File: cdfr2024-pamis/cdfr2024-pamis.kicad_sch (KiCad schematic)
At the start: 24 parts, among them J1 Connecteur batterie, J14 Conn_ST_STDC14, J4 Connecteur Programmation, J5 Connecteur Débug, J5 Connecteur ToF, J6 Moteur Droit, J7 Moteur Gauche, U1 LM317_SOT-223, U1 STM32F401RCTx, U4 Driver Moteur Droit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

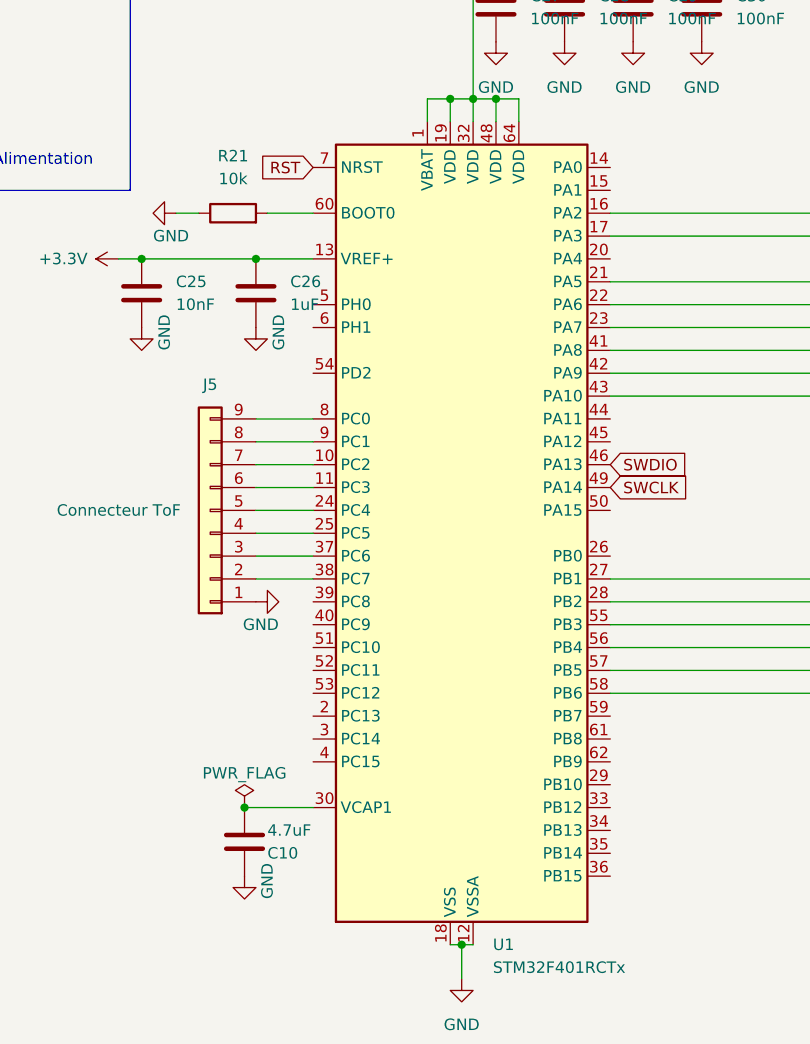
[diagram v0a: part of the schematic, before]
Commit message: - supression des messages d'erreur dans le schema - Suppression es message d'erreur sur PCB - modification des regles - modification du contour
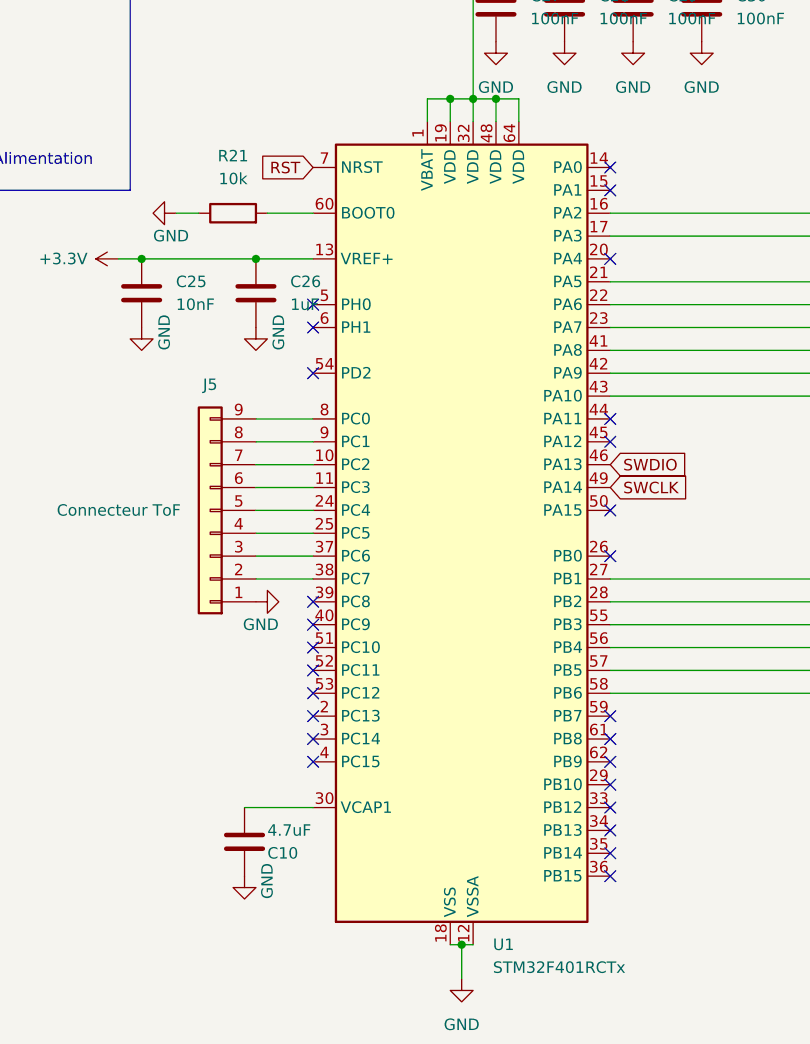
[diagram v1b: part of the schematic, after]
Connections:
- no-connect marks 4 -> 30
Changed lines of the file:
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@@
   (junction (at 146.05 46.99) (diameter 0) (color 0 0 0 0)
   )
-  (junction (at 123.19 125.73) (diameter 0) (color 0 0 0 0)
-  )
   (junction (at 60.96 48.26) (diameter 0) (color 0 0 0 0)
   )
@@
   (junction (at 34.29 25.4) (diameter 0) (color 0 0 0 0)
   )
+  (no_connect (at 163.83 118.11))
+  (no_connect (at 163.83 54.61))
+  (no_connect (at 163.83 115.57))
+  (no_connect (at 130.81 69.85))
   (no_connect (at 55.88 105.41))
+  (no_connect (at 130.81 105.41))
+  (no_connect (at 130.81 113.03))
+  (no_connect (at 163.83 97.79))
+  (no_connect (at 130.81 107.95))
+  (no_connect (at 163.83 82.55))
+  (no_connect (at 130.81 77.47))
+  (no_connect (at 130.81 118.11))
   (no_connect (at 71.12 92.71))
+  (no_connect (at 163.83 120.65))
+  (no_connect (at 163.83 57.15))
+  (no_connect (at 163.83 128.27))
+  (no_connect (at 163.83 85.09))
+  (no_connect (at 163.83 123.19))
+  (no_connect (at 163.83 64.77))
   (no_connect (at 71.12 87.63))
+  (no_connect (at 163.83 133.35))
+  (no_connect (at 163.83 125.73))
+  (no_connect (at 163.83 130.81))
+  (no_connect (at 163.83 92.71))
+  (no_connect (at 130.81 120.65))
+  (no_connect (at 130.81 102.87))
+  (no_connect (at 130.81 115.57))
   (no_connect (at 71.12 85.09))
+  (no_connect (at 130.81 110.49))
+  (no_connect (at 130.81 72.39))
   (wire (pts (xy 158.75 33.02) (xy 166.37 33.02))
     (stroke (width 0) (type default))
@@
         (path "/f2d064ab-e07d-4c4a-a207-b6758ac96116"
           (reference "#PWR010") (unit 1)
-        )
-      )
-    )
-  )
-  (symbol (lib_id "power:PWR_FLAG") (at 123.19 125.73 0) (unit 1)
-    (in_bom yes) (on_board yes) (dnp no)
-    (property "Reference" "#FLG0102" (at 123.19 123.825 0)
-      (effects (font (size 1.27 1.27)) hide)
-    )
-    (property "Value" "PWR_FLAG" (at 123.19 121.92 0)
-      (effects (font (size 1.27 1.27)))
-    )
-    (property "Footprint" "" (at 123.19 125.73 0)
-      (effects (font (size 1.27 1.27)) hide)
-    )
-    (property "Datasheet" "~" (at 123.19 125.73 0)
-      (effects (font (size 1.27 1.27)) hide)
-    )
-    (pin "1")
-    (instances
-      (project "Asservissement_CDFR_2023"
-        (path "/aba37299-4f54-471d-ab35-d760532fd54c"
-          (reference "#FLG0102") (unit 1)
-        )
-      )
-      (project "cdfr24_asservissement"
-        (path "/c6b82269-16f5-49e6-8b51-4d12a40a3077"
-          (reference "#FLG04") (unit 1)
-        )
-      )
-      (project "cdfr2024-pamis"
-        (path "/f2d064ab-e07d-4c4a-a207-b6758ac96116"
-          (reference "#FLG03") (unit 1)
         )
       )
@@
       (effects (font (size 1.27 1.27)) (justify bottom) hide)
     )
+    (pin "1")
+    (pin "10")
+    (pin "11")
+    (pin "12")
+    (pin "13")
+    (pin "14")
+    (pin "15")
+    (pin "16")
+    (pin "2")
     (pin "3")
-    (pin "15")
+    (pin "4")
+    (pin "5")
+    (pin "6")
     (pin "7")
-    (pin "12")
-    (pin "5")
-    (pin "1")
-    (pin "14")
-    (pin "11")
-    (pin "13")
-    (pin "16")
-    (pin "4")
     (pin "8")
-    (pin "2")
-    (pin "10")
-    (pin "6")
     (pin "9")
     (instances
@@
       (effects (font (size 1.27 1.27)) hide)
     )
-    (pin "2")
+    (pin "1")
+    (pin "2")
+    (pin "3")
     (pin "4")
-    (pin "3")
-    (pin "1")
     (instances
       (project "cdfr2024-pamis"
@@
       (effects (font (size 1.27 1.27)) hide)
     )
+    (pin "1")
+    (pin "10")
+    (pin "11")
+    (pin "12")
+    (pin "13")
+    (pin "14")
+    (pin "15")
+    (pin "16")
+    (pin "17")
+    (pin "18")
+    (pin "19")
+    (pin "2")
+    (pin "20")
+    (pin "21")
     (pin "22")
-    (pin "18")
+    (pin "23")
+    (pin "24")
+    (pin "25")
+    (pin "26")
     (pin "27")
+    (pin "28")
+    (pin "29")
+    (pin "3")
+    (pin "30")
+    (pin "31")
+    (pin "32")
+    (pin "33")
+    (pin "34")
     (pin "35")
     (pin "36")
-    (pin "3")
-    (pin "58")
-    (pin "10")
-    (pin "21")
+    (pin "37")
+    (pin "38")
+    (pin "39")
+    (pin "4")
+    (pin "40")
+    (pin "41")
+    (pin "42")
     (pin "43")
-    (pin "42")
-    (pin "6")
-    (pin "12")
-    (pin "62")
+    (pin "44")
+    (pin "45")
+    (pin "46")
+    (pin "47")
+    (pin "48")
     (pin "49")
-    (pin "54")
-    (pin "57")
-    (pin "61")
-    (pin "20")
-    (pin "16")
-    (pin "28")
-    (pin "30")
-    (pin "25")
-    (pin "4")
-    (pin "37")
-    (pin "39")
-    (pin "40")
-    (pin "48")
-    (pin "29")
-    (pin "14")
-    (pin "15")
-    (pin "31")
-    (pin "47")
+    (pin "5")
     (pin "50")
     (pin "51")
-    (pin "26")
-    (pin "33")
-    (pin "24")
     (pin "52")
-    (pin "46")
-    (pin "2")
-    (pin "17")
-    (pin "23")
-    (pin "45")
-    (pin "5")
+    (pin "53")
+    (pin "54")
+    (pin "55")
     (pin "56")
+    (pin "57")
+    (pin "58")
     (pin "59")
+    (pin "6")
     (pin "60")
+    (pin "61")
+    (pin "62")
+    (pin "63")
     (pin "64")
     (pin "7")
-    (pin "34")
-    (pin "19")
-    (pin "1")
-    (pin "32")
-    (pin "41")
-    (pin "53")
     (pin "8")
-    (pin "44")
-    (pin "38")
-    (pin "11")
-    (pin "13")
-    (pin "55")
-    (pin "63")
     (pin "9")
     (instances
@@
       (effects (font (size 1.27 1.27)) hide)
     )
+    (pin "1")
+    (pin "2")
     (pin "3")
+    (pin "4")
     (pin "5")
     (pin "6")
-    (pin "1")
-    (pin "4")
     (pin "7")
-    (pin "2")
+    (pin "8")
     (pin "9")
-    (pin "8")
     (instances
       (project "cdfr2024-pamis"
@@
       (effects (font (size 1.27 1.27)) (justify bottom) hide)
     )
+    (pin "1")
+    (pin "10")
+    (pin "11")
+    (pin "12")
+    (pin "13")
+    (pin "14")
+    (pin "15")
+    (pin "16")
+    (pin "2")
     (pin "3")
-    (pin "15")
+    (pin "4")
+    (pin "5")
+    (pin "6")
     (pin "7")
-    (pin "12")
-    (pin "5")
-    (pin "1")
-    (pin "14")
-    (pin "11")
-    (pin "13")
-    (pin "16")
-    (pin "4")
     (pin "8")
-    (pin "2")
-    (pin "10")
-    (pin "6")
     (pin "9")
     (instances

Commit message: module wifi
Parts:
- removed C10: 4.7uF, Capacitor_SMD:C_0805_2012Metric_Pad1.18x1.45mm_HandSolder, symbol Device:C
- removed C25: 10nF, Capacitor_SMD:C_0805_2012Metric_Pad1.18x1.45mm_HandSolder, symbol Device:C
- removed C26: 1uF, Capacitor_SMD:C_0805_2012Metric_Pad1.18x1.45mm_HandSolder, symbol Device:C
- removed C27, C28, C29, C30: 100nF, Capacitor_SMD:C_0805_2012Metric_Pad1.18x1.45mm_HandSolder, symbol Device:C
- removed J14: Conn_ST_STDC14, FTSH-107-01-L-DV-K-A:SAMTEC_FTSH-107-01-L-DV-K-A, symbol Connector:Conn_ST_STDC14
- removed J4: Connecteur Programmation, Connector_PinHeader_2.54mm:PinHeader_1x04_P2.54mm_Vertical, symbol Connector_Generic:Conn_01x04
- removed J5: Connecteur Débug, Connector_PinHeader_2.54mm:PinHeader_1x03_P2.54mm_Vertical, symbol Connector_Generic:Conn_01x03
- removed R21: 10k, Resistor_SMD:R_0805_2012Metric_Pad1.20x1.40mm_HandSolder, symbol Device:R
- removed U1: STM32F401RCTx, Package_QFP:LQFP-64_10x10mm_P0.5mm, symbol MCU_ST_STM32F4:STM32F401RCTx
- added U3: ESP32-S3-DEVKITC-1-N8R2, ESP32S3-devkit:ESP32-S3-DEVKITC, symbol ESP32-S3-DEVKITC-1-N8R2:ESP32-S3-DEVKITC-1-N8R2
- U4, U5: footprint A4988_Stepper_Motor_Driver:MODULE_A4988_STEPPER_MOTOR_DRIVER_CARRIER -> A4988:MODULE_A4988_STEPPER_MOTOR_DRIVER_CARRIER
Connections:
- net +3.3V: now also U3.J1_1 (3V3), U3.J1_2 (3V3)
- net GND: now also U3.J1_22 (GND), U3.J3_1 (GND), U3.J3_21 (GND), U3.J3_22 (GND)
- net at U4.1 (DIR): now also U3.J1_15 (GPIO9)
- net at U4.2 (STEP): now also U3.J1_16 (GPIO10)
- net at U4.5 (M2): now also U3.J1_17 (GPIO11)
- net at U4.6 (M1): now also U3.J1_18 (GPIO12)
- net at U4.7 (M0): now also U3.J1_19 (GPIO13)
- net at U4.8 (~{ENABLE}): now also U3.J1_20 (GPIO14)
- net at J5.7 (Pin_7): now also U3.J3_11 (GPIO37)
- net at J5.6 (Pin_6): now also U3.J3_10 (GPIO38)
- net at U5.1 (DIR): now also U3.J3_14 (GPIO0)
- net at U5.2 (STEP): now also U3.J3_4 (GPIO1)
- net at U5.5 (M2): now also U3.J3_5 (GPIO2)
- net at J5.5 (Pin_5): now also U3.J3_15 (GPIO45)
- net at J5.4 (Pin_4): now also U3.J1_14 (GPIO46)
- net at J5.3 (Pin_3): now also U3.J3_17 (GPIO47)
- net at J5.2 (Pin_2): now also U3.J3_16 (GPIO48)
- net at U5.6 (M1): now also U3.J1_13 (GPIO3)
- net at U5.7 (M0): now also U3.J1_4 (GPIO4)
- net at U5.8 (~{ENABLE}): now also U3.J1_5 (GPIO5)
- net at J5.9 (Pin_9): now also U3.J3_13 (GPIO35)
- net at J5.8 (Pin_8): now also U3.J3_12 (GPIO36)
- no-connect marks 30 -> 18
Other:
- moved on the sheet: J5, J6, J7, U4, U5

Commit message: Routage + DRC
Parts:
- removed J6: Moteur Droit, Connector_PinHeader_2.54mm:PinHeader_1x04_P2.54mm_Vertical, symbol Connector_Generic:Conn_01x04
- added J3: Connecteur RF, Connector_PinHeader_2.54mm:PinHeader_1x04_P2.54mm_Vertical, symbol Connector_Generic:Conn_01x04
- added J4: Moteur Droit, Connector_PinHeader_2.54mm:PinHeader_1x04_P2.54mm_Vertical, symbol Connector_Generic:Conn_01x04
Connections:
- net +7.5V: now also J3.1 (Pin_1)
- net GND: now also J3.4 (Pin_4)
- net at U4.1 (DIR): now also U3.J1_17 (GPIO11); no longer U3.J1_15 (GPIO9)
- net at U4.11 (A1): now also J4.4 (Pin_4)
- net at U4.12 (A2): now also J4.3 (Pin_3)
- net at U4.13 (B2): now also J4.2 (Pin_2)
- net at U4.14 (B1): now also J4.1 (Pin_1)
- net at U4.2 (STEP): now also U3.J1_18 (GPIO12); no longer U3.J1_16 (GPIO10)
- net at U4.5 (M2): no longer U3.J1_17 (GPIO11)
- net at U4.6 (M1): no longer U3.J1_18 (GPIO12)
- net at U4.7 (M0): no longer U3.J1_19 (GPIO13)
- net at U4.8 (~{ENABLE}): now also U3.J1_19 (GPIO13); no longer U3.J1_20 (GPIO14)
- net at U5.5 (M2): no longer U3.J3_5 (GPIO2)
- net at U5.6 (M1): no longer U3.J1_13 (GPIO3)
- net at U5.7 (M0): no longer U3.J1_4 (GPIO4)
- net at U5.8 (~{ENABLE}): now also U3.J3_5 (GPIO2); no longer U3.J1_5 (GPIO5)
- net at U3.J3_2 (U0TXD/GPIO43): now also J3.3 (Pin_3)
- net at U3.J3_3 (U0RXD/GPIO44): now also J3.2 (Pin_2)
- no-connect marks 18 -> 13

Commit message: carte fablab module rf
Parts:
- removed J3: Connecteur RF, Connector_PinHeader_2.54mm:PinHeader_1x04_P2.54mm_Vertical, symbol Connector_Generic:Conn_01x04
- removed U3: ESP32-S3-DEVKITC-1-N8R2, ESP32S3-devkit:ESP32-S3-DEVKITC, symbol ESP32-S3-DEVKITC-1-N8R2:ESP32-S3-DEVKITC-1-N8R2
- added J2: Connecteur Bouton, Connector_PinHeader_2.54mm:PinHeader_1x02_P2.54mm_Vertical, symbol Connector_Generic:Conn_01x02
- added J8: Connecteur RF, Connector_PinHeader_2.54mm:PinHeader_1x08_P2.54mm_Vertical, symbol Connector_Generic:Conn_01x08
- added U1: ESP32-DEVKIT-V1, ESP32DevkitV1:MODULE_ESP32_DEVKIT_V1, symbol ESP32-DEVKIT-V1:ESP32-DEVKIT-V1
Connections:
- net +3.3V is gone; now on net +3V3: C11.1, D1.2 (A), R2.1, U1.2 (VO), U4.10 (VDD), U5.10 (VDD)
- net +7.5V: now also J2.2 (Pin_2); no longer J1.1 (Pin_1)
- net GND: now also J8.8 (Pin_8), U1.2 (GND), U1.29 (GND)
- net at U4.1 (DIR): now also U1.26 (D14)
- net at U4.2 (STEP): now also U1.28 (D13)
- net at U4.8 (~{ENABLE}): now also U1.27 (D12)
- net at U5.1 (DIR): now also U1.8 (D5)
- net at U5.2 (STEP): now also U1.5 (D4)
- net at U5.8 (~{ENABLE}): now also U1.4 (D2)
- net at J5.4 (Pin_4): now also U1.25 (D27)
- net SCL: now reaches J5.6 (Pin_6)
- net SCL: now also U1.14 (D22)
- net SDA: now reaches J5.7 (Pin_7)
- net SDA: now also U1.11 (D21)
- net at J5.8 (Pin_8): now also U1.23 (D25)
- net at J5.9 (Pin_9): now also U1.22 (D33)
- net at J5.5 (Pin_5): now also U1.24 (D26)
- net +3V3: now reaches J5.2 (Pin_2)
- net +3V3: now also J5.3 (Pin_3), J8.7 (Pin_7), U1.1 (3V3), U1.16 (EN), U1.30 (VIN)
- new net: J8.1 (Pin_1), U1.21 (D32)
- new net: J8.2 (Pin_2), U1.20 (D35)
- new net: J8.3 (Pin_3), U1.19 (D34)
- new net: J1.1 (Pin_1), J2.1 (Pin_1)
- new net SCLK: J8.4 (Pin_4), U1.9 (D18)
- new net SDI: J8.5 (Pin_5), U1.10 (D19)
- new net SDO: J8.6 (Pin_6), U1.15 (D23)
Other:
- note added: "Nc button"
- note added: "mosi sdo miso sdi"
- moved on the sheet: J4, J5, U4

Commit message: carte pamis
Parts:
- removed C11: 100uF, Capacitor_SMD:CP_Elec_10x10.5, symbol Device:C_Polarized
- removed D1: LED, LED_SMD:LED_0805_2012Metric_Pad1.15x1.40mm_HandSolder, symbol Device:LED
- removed J8: Connecteur RF, Connector_PinHeader_2.54mm:PinHeader_1x08_P2.54mm_Vertical, symbol Connector_Generic:Conn_01x08
- removed R2: 2k4, Resistor_SMD:R_0805_2012Metric_Pad1.20x1.40mm_HandSolder, symbol Device:R
- removed R3: 150, Resistor_SMD:R_0805_2012Metric_Pad1.20x1.40mm_HandSolder, symbol Device:R
- removed R4: 3k9, Resistor_SMD:R_0805_2012Metric_Pad1.20x1.40mm_HandSolder, symbol Device:R
- removed U1: LM317_SOT-223, Package_TO_SOT_SMD:SOT-223-3_TabPin2, symbol Regulator_Linear:LM317_SOT-223
- added J3: Connecteur RF, Connector_PinHeader_2.54mm:PinHeader_1x12_P2.54mm_Vertical, symbol Connector_Generic:Conn_01x12
- added J6: Module MP1584EN, MP1584EN_Module:SRT_MPT1584EN_Module, symbol Connector_Generic:Conn_01x04
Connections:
- net +3V3: now also J3.8 (Pin_8), J6.3 (Pin_3); no longer U1.16 (EN), U1.30 (VIN)
- net +7.5V: now also J6.1 (Pin_1)
- net GND: now also J3.1 (Pin_1), J3.12 (Pin_12), J6.2 (Pin_2), J6.4 (Pin_4)
- net DR_DIRD: now reaches U4.1 (DIR)
- net DR_DIRD: now also U1.22 (D33); no longer U1.26 (D14)
- net DR_STEPD: now reaches U4.2 (STEP)
- net DR_STEPD: now also U1.21 (D32); no longer U1.28 (D13)
- net at U4.3: now also U4.4
- net at U4.8 (~{ENABLE}): no longer U1.27 (D12)
- net EVK_INT: now reaches J5.9 (Pin_9)
- net EVK_INT: now also U1.28 (D13); no longer U1.22 (D33)
- net DR_STEPG: now reaches U1.23 (D25)
- net DR_STEPG: now also U5.2 (STEP); no longer J5.8 (Pin_8)
- net DR_DIRG: now reaches U1.24 (D26)
- net DR_DIRG: now also U5.1 (DIR); no longer J5.5 (Pin_5)
- net EVK_EN: now reaches J5.4 (Pin_4), U1.25 (D27)
- net at U5.8 (~{ENABLE}): no longer U1.4 (D2)
- net RF_3: now reaches U1.5 (D4)
- net RF_3: now also J3.3 (Pin_3); no longer U5.2 (STEP)
- net RF_4: now reaches U1.8 (D5)
- net RF_4: now also J3.4 (Pin_4); no longer U5.1 (DIR)
- net at U5.3: now also U5.4
- net SCL renamed EVK_SCL
- net SCLK renamed RF_SCLK
- net RF_SCLK: now also J3.5 (Pin_5)
- net SDA renamed EVK_SDA
- net SDI renamed RF_SDI
- net RF_SDI: now also J3.6 (Pin_6)
- net SDO renamed RF_SDO
- net RF_SDO: now also J3.7 (Pin_7)
- new net EVK_LPN: J5.5 (Pin_5), U1.26 (D14)
- new net EVK_RST: J5.8 (Pin_8), U1.27 (D12)
- new net RF_2: J3.2 (Pin_2), U1.4 (D2)
- no-connect marks 13 -> 22
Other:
- moved on the sheet: J1, J2, J4, J5, J7, U4, U5
